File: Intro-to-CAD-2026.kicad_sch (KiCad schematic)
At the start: 8 parts

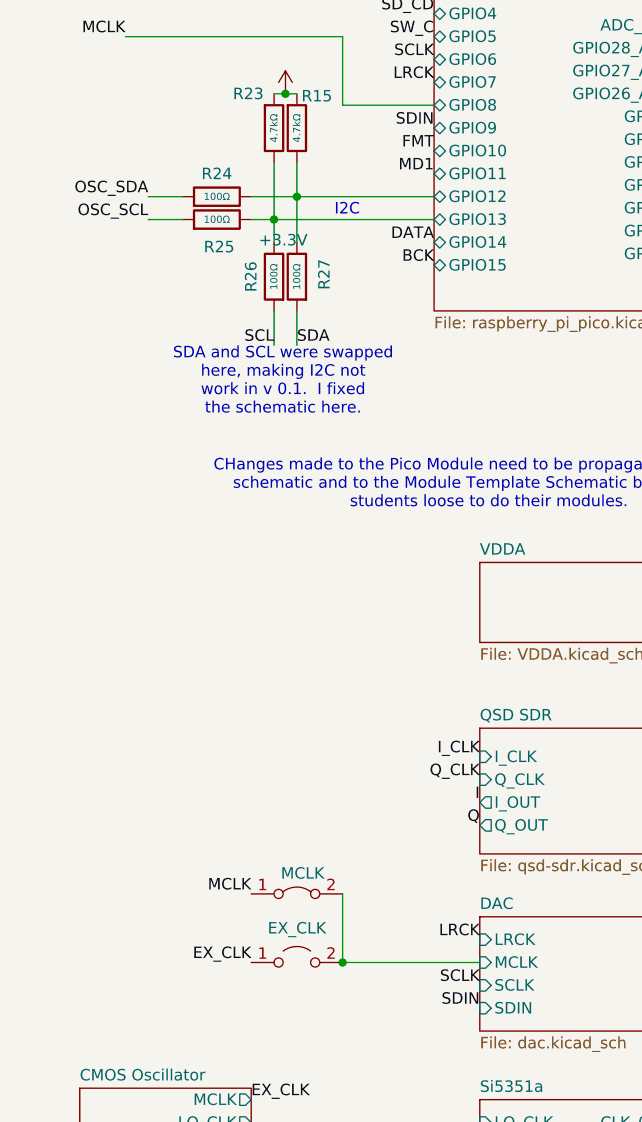
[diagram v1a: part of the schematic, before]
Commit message: Starting a new branch for v0.2
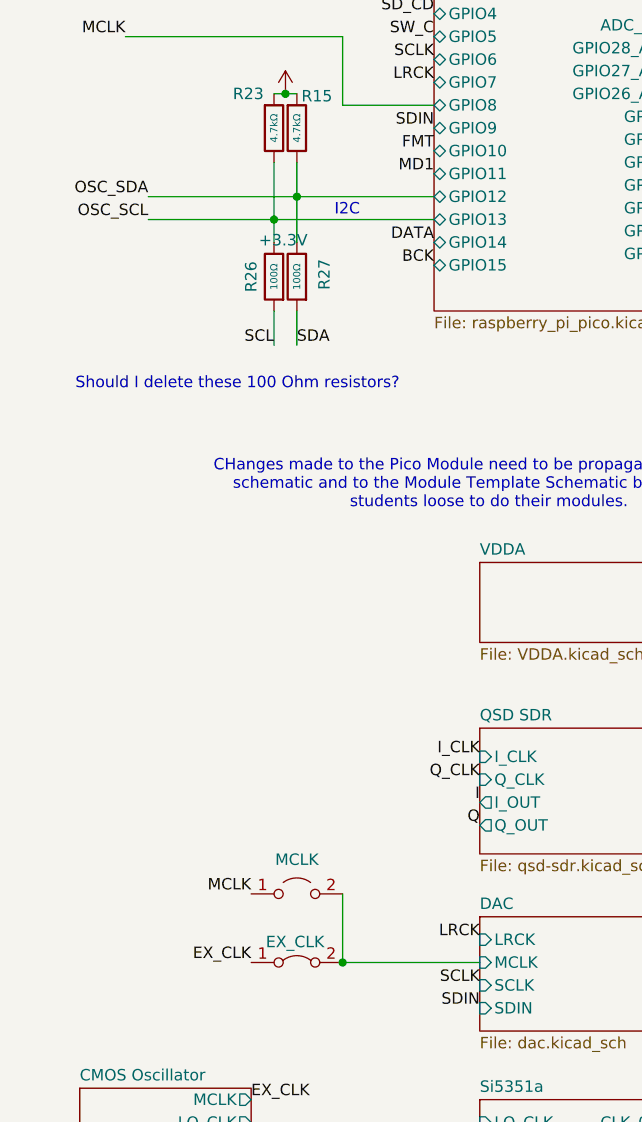
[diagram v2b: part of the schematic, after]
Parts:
- removed R24, R25: 100Ω, PCM_JLCPCB:R_0805, symbol PCM_JLCPCB-Resistors:0805,100Ω
- JP6: value EX_CLK -> MCLK
- e9: value MCLK -> EX_CLK
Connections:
- net Raspberry_Pi_Pico/GPIO12 is gone; now on net OSC_SDA: R15.2, R27.2
- net Raspberry_Pi_Pico/GPIO13 is gone; now on net OSC_SCL: R23.2, R26.2
- net EX_CLK: now also e9.1 (A); no longer JP6.1 (A)
- net MCLK: now also JP6.1 (A); no longer e9.1 (A)
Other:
- note added: "Should I delete these 100 Ohm resistors?"
- note removed: "SDA and SCL were swapped here, making I2C not work in v 0.1. I fixed the schematic here."

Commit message: Added CJC5340
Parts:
- removed JP6: MCLK, Jumper:SolderJumper-2_P1.3mm_Open_RoundedPad1.0x1.5mm, symbol Jumper:Jumper_2_Open
- removed e9: EX_CLK, Jumper:SolderJumper-2_P1.3mm_Bridged_RoundedPad1.0x1.5mm, symbol Jumper:Jumper_2_Bridged
- added JP11, JP12, JP13, JP14, JP6: Clock Select, Jumper:SolderJumper-3_P1.3mm_Bridged12_RoundedPad1.0x1.5mm_NumberLabels, symbol Jumper:Jumper_3_Bridged12
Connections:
- net +3.3V: now also JP11.3 (B), JP12.3 (B), JP13.3 (B), JP14.3 (B)
- net DAC/MCLK: now also JP6.2 (C)
- net EX_CLK: now also JP6.1 (A)
- net FMT: now also JP13.2 (C)
- net MD1: now also JP14.2 (C)
- new net GND: JP11.1 (A), JP12.1 (A), JP13.1 (A), JP14.1 (A)
- new net M0: JP11.2 (C)
- new net M1: JP12.2 (C)
- new net PICO_MCLK: JP6.3 (B)
- no-connect marks 4 -> 3
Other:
- added sheet CJC5340 (CJC5340.kicad_sch)
- sheet CMOS Oscillator ports: added SCKI1, SCKI2; removed SCKI
- sheet PCM1808 ports: added OUT_L, OUT_R; removed none
- note added: "48 kHz default"
- note added: "I2S Format (FMT) 48 kHz (MD1) default"

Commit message: More edits....
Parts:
- JP11: value Clock Select -> M0
- JP12: value Clock Select -> M1
- JP13: value Clock Select -> FMT
- JP14: value Clock Select -> MD1
- JP6: value Clock Select -> DAC MCLK
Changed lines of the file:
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@@
 		(property "Reference" "JP11"
 			(at 199.644 140.97 90)
+			(hide yes)
 			(show_name no)
 			(do_not_autoplace no)
@@
 			)
 		)
-		(property "Value" "Clock Select"
+		(property "Value" "M0"
 			(at 190.5 146.0499 90)
-			(hide yes)
 			(show_name no)
 			(do_not_autoplace no)
@@
 		(property "Reference" "JP12"
 			(at 216.154 140.97 90)
+			(hide yes)
 			(show_name no)
 			(do_not_autoplace no)
@@
 			)
 		)
-		(property "Value" "Clock Select"
+		(property "Value" "M1"
 			(at 207.01 146.0499 90)
-			(hide yes)
 			(show_name no)
 			(do_not_autoplace no)
@@
 		(property "Reference" "JP14"
 			(at 96.266 182.88 90)
+			(hide yes)
 			(show_name no)
 			(do_not_autoplace no)
@@
 			)
 		)
-		(property "Value" "Clock Select"
-			(at 105.41 187.9599 90)
-			(hide yes)
+		(property "Value" "MD1"
+			(at 97.536 188.722 90)
 			(show_name no)
 			(do_not_autoplace no)
@@
 		(property "Reference" "JP6"
 			(at 49.784 137.16 90)
+			(hide yes)
 			(show_name no)
 			(do_not_autoplace no)
@@
 			)
 		)
-		(property "Value" "Clock Select"
+		(property "Value" "DAC MCLK"
 			(at 40.64 142.2399 90)
-			(hide yes)
 			(show_name no)
 			(do_not_autoplace no)
@@
 		(property "Reference" "JP13"
 			(at 112.776 182.88 90)
+			(hide yes)
 			(show_name no)
 			(do_not_autoplace no)
@@
 			)
 		)
-		(property "Value" "Clock Select"
-			(at 121.92 187.9599 90)
-			(hide yes)
-			(show_name no)
-			(do_not_autoplace no)
+		(property "Value" "FMT"
+			(at 114.3 188.976 90)
+			(show_name no)
+			(do_not_autoplace no)

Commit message: Placed the second ADC
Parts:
- R15, R23, R26, R27: Manufacturer UNI-ROYAL(Uniroyal Elec) -> (none)
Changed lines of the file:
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@@
 		)
 	)
-	(label "FMT{slash}M0"
+	(label "FMT"
 		(at 82.55 177.8 0)
 		(effects
@@
 		)
 	)
-	(label "MD1{slash}M1"
+	(label "MD1"
 		(at 62.23 179.07 180)
 		(effects
@@
 			)
 		)
-		(property "Manufacturer" "UNI-ROYAL(Uniroyal Elec)"
-			(at 41.91 64.77 0)
-			(hide yes)
-			(show_name no)
-			(do_not_autoplace no)
-			(effects
-				(font
-					(size 1.27 1.27)
-				)
-			)
-		)
 		(property "Part" "0805W8F1000T5E"
 			(at 41.91 64.77 0)
@@
 		)
 		(property "Category" "Resistors,Chip Resistor - Surface Mount"
-			(at 39.37 48.26 0)
-			(hide yes)
-			(show_name no)
-			(do_not_autoplace no)
-			(effects
-				(font
-					(size 1.27 1.27)
-				)
-			)
-		)
-		(property "Manufacturer" "UNI-ROYAL(Uniroyal Elec)"
 			(at 39.37 48.26 0)
 			(hide yes)
@@
 		)
 		(property "Category" "Resistors,Chip Resistor - Surface Mount"
-			(at 39.37 64.77 0)
-			(hide yes)
-			(show_name no)
-			(do_not_autoplace no)
-			(effects
-				(font
-					(size 1.27 1.27)
-				)
-			)
-		)
-		(property "Manufacturer" "UNI-ROYAL(Uniroyal Elec)"
 			(at 39.37 64.77 0)
 			(hide yes)
@@
 			(at 41.91 48.26 0)
 			(hide yes)
-			(show_name no)
-			(do_not_autoplace no)
-			(effects
-				(font
-					(size 1.27 1.27)
-				)
-			)
-		)
-		(property "Manufacturer" "UNI-ROYAL(Uniroyal Elec)"
-			(at 41.91 48.26 0)
-			(hide yes)
